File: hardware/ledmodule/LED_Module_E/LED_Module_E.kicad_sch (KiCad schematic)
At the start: 86 parts, among them J1 USB4125-GF-A, J2 Conn_02x11_Odd_Even, Q1 Si3456DDV, Q11 Si3456DDV, Q12 Si3456DDV, Q2 Si3456DDV, Q3 Si3456DDV, Q4 Si3456DDV, Q5 Si3456DDV, Q6 Si3456DDV, Q7 Si3456DDV, Q8 Si3456DDV, U1 TMP1075DGK, U2 74HCT244, U3 24AA02UIDT-I/OT

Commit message: Fix / add meta data in title_block for all LED modules.
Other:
- title: (none) -> besteLampe! LED Module E
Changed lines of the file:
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@@
 	(generator_version "8.0")
 	(paper "A4")
+	(title_block
+		(title "besteLampe! LED Module E")
+		(date "2024-07-01")
+		(rev "1.0")
+		(comment 1 "See  https://lenaschimmel.de/besteLampe! for the source and more information")
+		(comment 2 "This source describes Open Hardware and is licensed under the CERN-OHL-S v2.")
+		(comment 3 "Copyright 2024 Lena Schimmel <mail@lenaschimmel.de>")
+	)
 	(junction
 		(at 160.655 138.43)

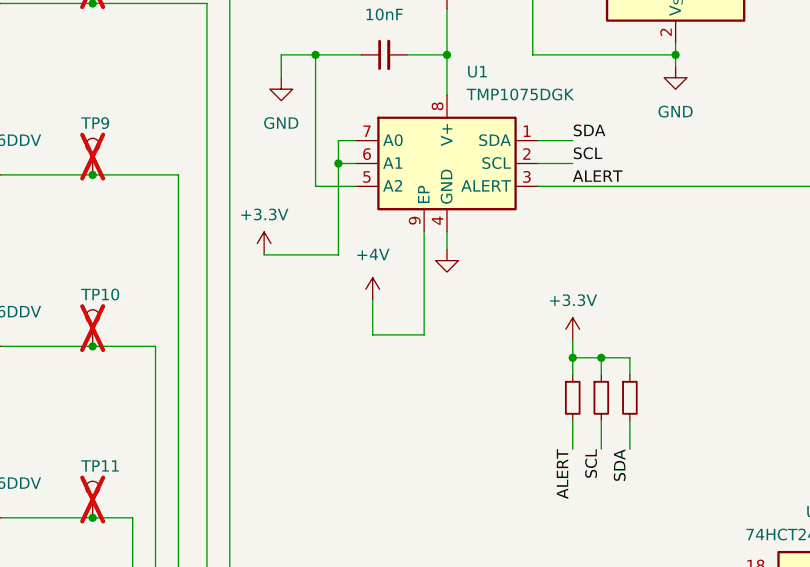
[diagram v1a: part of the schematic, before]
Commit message: Probably minor changes (specific R values, etc.)
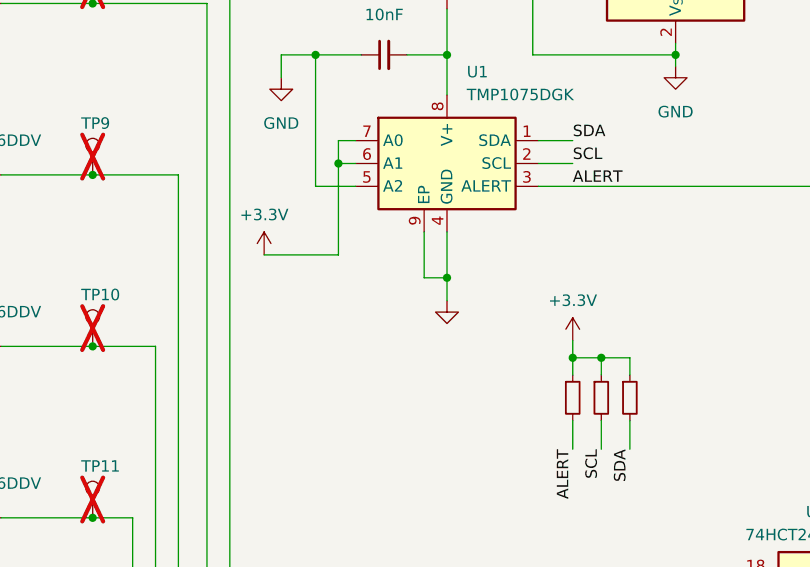
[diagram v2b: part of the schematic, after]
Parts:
- R10, R13, R14, R15, R16, R17, R18, R19, R20, R21, R22, R23, R24, R25, R26, R27, R28, R29, R30, R9: value R_Small -> 2740R
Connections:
- net +4V: no longer U1.9 (EP)
- net GND: now also U1.9 (EP)
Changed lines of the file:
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@@
 	)
 	(junction
+		(at 146.05 76.2)
+		(diameter 0)
+		(color 0 0 0 0)
+	)
+	(junction
 		(at 226.06 116.84)
 		(diameter 0)
@@
 	(wire
 		(pts
+			(xy 143.51 76.2) (xy 146.05 76.2)
+		)
+		(stroke
+			(width 0)
+			(type default)
+		)
+	)
+	(wire
+		(pts
 			(xy 171.45 50.165) (xy 171.45 51.435)
 		)
@@
 	(wire
 		(pts
+			(xy 146.05 76.2) (xy 146.05 78.74)
+		)
+		(stroke
+			(width 0)
+			(type default)
+		)
+	)
+	(wire
+		(pts
 			(xy 147.955 114.3) (xy 116.205 114.3)
 		)
@@
 	(wire
 		(pts
-			(xy 137.795 82.55) (xy 137.795 78.74)
-		)
-		(stroke
-			(width 0)
-			(type default)
-		)
-	)
-	(wire
-		(pts
 			(xy 67.31 76.2) (xy 81.915 76.2)
 		)
@@
 	(wire
 		(pts
-			(xy 143.51 82.55) (xy 137.795 82.55)
-		)
-		(stroke
-			(width 0)
-			(type default)
-		)
-	)
-	(wire
-		(pts
 			(xy 203.2 111.76) (xy 219.71 111.76)
 		)
@@
 	(wire
 		(pts
-			(xy 143.51 71.12) (xy 143.51 82.55)
-		)
-		(stroke
-			(width 0)
-			(type default)
-		)
-	)
-	(wire
-		(pts
 			(xy 144.78 135.89) (xy 144.78 138.43)
 		)
@@
 	(wire
 		(pts
+			(xy 143.51 71.12) (xy 143.51 76.2)
+		)
+		(stroke
+			(width 0)
+			(type default)
+		)
+	)
+	(wire
+		(pts
 			(xy 222.885 114.3) (xy 222.885 130.81)
 		)
@@
 	(wire
 		(pts
-			(xy 146.05 71.12) (xy 146.05 73.025)
+			(xy 146.05 71.12) (xy 146.05 76.2)
 		)
 		(stroke
@@
 			)
 		)
-		(property "Value" "R_Small"
+		(property "Value" "2740R"
 			(at 209.5499 136.525 0)
 			(effects
@@
 			)
 		)
-		(property "Value" "R_Small"
+		(property "Value" "2740R"
 			(at 150.495 134.6199 0)
 			(effects
@@
 			)
 		)
-		(property "Value" "R_Small"
+		(property "Value" "2740R"
 			(at 153.67 134.6199 0)
 			(effects
@@
 	)
 	(symbol
-		(lib_id "power:+4V")
-		(at 137.795 78.74 0)
-		(unit 1)
-		(exclude_from_sim no)
-		(in_bom yes)
-		(on_board yes)
-		(dnp no)
-		(fields_autoplaced yes)
-		(property "Reference" "#PWR017"
-			(at 137.795 82.55 0)
-			(effects
-				(font
-					(size 1.27 1.27)
-				)
-				(hide yes)
-			)
-		)
-		(property "Value" "+4V"
-			(at 137.795 73.66 0)
-			(effects
-				(font
-					(size 1.27 1.27)
-				)
-			)
-		)
-		(property "Footprint" ""
-			(at 137.795 78.74 0)
-			(effects
-				(font
-					(size 1.27 1.27)
-				)
-				(hide yes)
-			)
-		)
-		(property "Datasheet" ""
-			(at 137.795 78.74 0)
-			(effects
-				(font
-					(size 1.27 1.27)
-				)
-				(hide yes)
-			)
-		)
-		(property "Description" "Power symbol creates a global label with name \"+4V\""
-			(at 137.795 78.74 0)
-			(effects
-				(font
-					(size 1.27 1.27)
-				)
-				(hide yes)
-			)
-		)
-		(pin "1"
-		)
-		(instances
-			(project "LED_Module_E"
-				(path "/271a71a9-d0cc-4466-ad75-113fb931f3c8"
-					(reference "#PWR017")
-					(unit 1)
-				)
-			)
-		)
-	)
-	(symbol
 		(lib_id "Device:R")
 		(at 76.2 116.84 90)
@@
 			)
 		)
-		(property "Value" "R_Small"
+		(property "Value" "2740R"
 			(at 168.91 90.8049 0)
 			(effects
@@
 			)
 		)
-		(property "Value" "R_Small"
+		(property "Value" "2740R"
 			(at 234.95 134.6199 0)
 			(effects
@@
 			)
 		)
-		(property "Value" "R_Small"
+		(property "Value" "2740R"
 			(at 166.37 134.6199 0)
 			(effects
@@
 			)
 		)
-		(property "Value" "R_Small"
+		(property "Value" "2740R"
 			(at 228.6 134.6199 0)
 			(effects
@@
 			)
 		)
-		(property "Value" "R_Small"
+		(property "Value" "2740R"
 			(at 165.735 90.8049 0)
 			(effects
@@
 			)
 		)
-		(property "Value" "R_Small"
+		(property "Value" "2740R"
 			(at 162.56 90.8049 0)
 			(effects
@@
 			)
 		)
-		(property "Value" "R_Small"
+		(property "Value" "2740R"
 			(at 238.125 134.6199 0)
 			(effects
@@
 	(symbol
 		(lib_id "power:GND")
-		(at 146.05 73.025 0)
+		(at 146.05 78.74 0)
 		(unit 1)
 		(exclude_from_sim no)
@@
 		(fields_autoplaced yes)
 		(property "Reference" "#PWR01"
-			(at 146.05 79.375 0)
+			(at 146.05 85.09 0)
 			(effects
 				(font
@@
 		)
 		(property "Value" "GND"
-			(at 146.05 78.105 0)
+			(at 146.05 83.82 0)
 			(effects
 				(font
@@
 		)
 		(property "Footprint" ""
-			(at 146.05 73.025 0)
+			(at 146.05 78.74 0)
 			(effects
 				(font
@@
 		)
 		(property "Datasheet" ""
-			(at 146.05 73.025 0)
+			(at 146.05 78.74 0)
 			(effects
 				(font
@@
 		)
 		(property "Description" "Power symbol creates a global label with name \"GND\" , ground"
-			(at 146.05 73.025 0)
+			(at 146.05 78.74 0)
 			(effects
 				(font
@@
 			)
 		)
-		(property "Value" "R_Small"
+		(property "Value" "2740R"
 			(at 225.425 134.6199 0)
 			(effects
@@
 			)
 		)
-		(property "Value" "R_Small"
+		(property "Value" "2740R"
 			(at 144.145 134.6199 0)
 			(effects
@@
 			)
 		)
-		(property "Value" "R_Small"
+		(property "Value" "2740R"
 			(at 160.02 134.6199 0)
 			(effects
@@
 			)
 		)
-		(property "Value" "R_Small"
+		(property "Value" "2740R"
 			(at 222.25 134.6199 0)
 			(effects
@@
 			)
 		)
-		(property "Value" "R_Small"
+		(property "Value" "2740R"
 			(at 147.32 134.6199 0)
 			(effects
@@
 			)
 		)
-		(property "Value" "R_Small"
+		(property "Value" "2740R"
 			(at 156.845 134.6199 0)
 			(effects
@@
 			)
 		)
-		(property "Value" "R_Small"
+		(property "Value" "2740R"
 			(at 219.075 134.6199 0)
 			(effects
@@
 			)
 		)
-		(property "Value" "R_Small"
+		(property "Value" "2740R"
 			(at 163.195 134.6199 0)
 			(effects
@@
 			)
 		)
-		(property "Value" "R_Small"
+		(property "Value" "2740R"
 			(at 231.775 134.6199 0)
 			(effects
@@
 			)
 		)
-		(property "Value" "R_Small"
+		(property "Value" "2740R"
 			(at 241.3 134.6199 0)
 			(effects

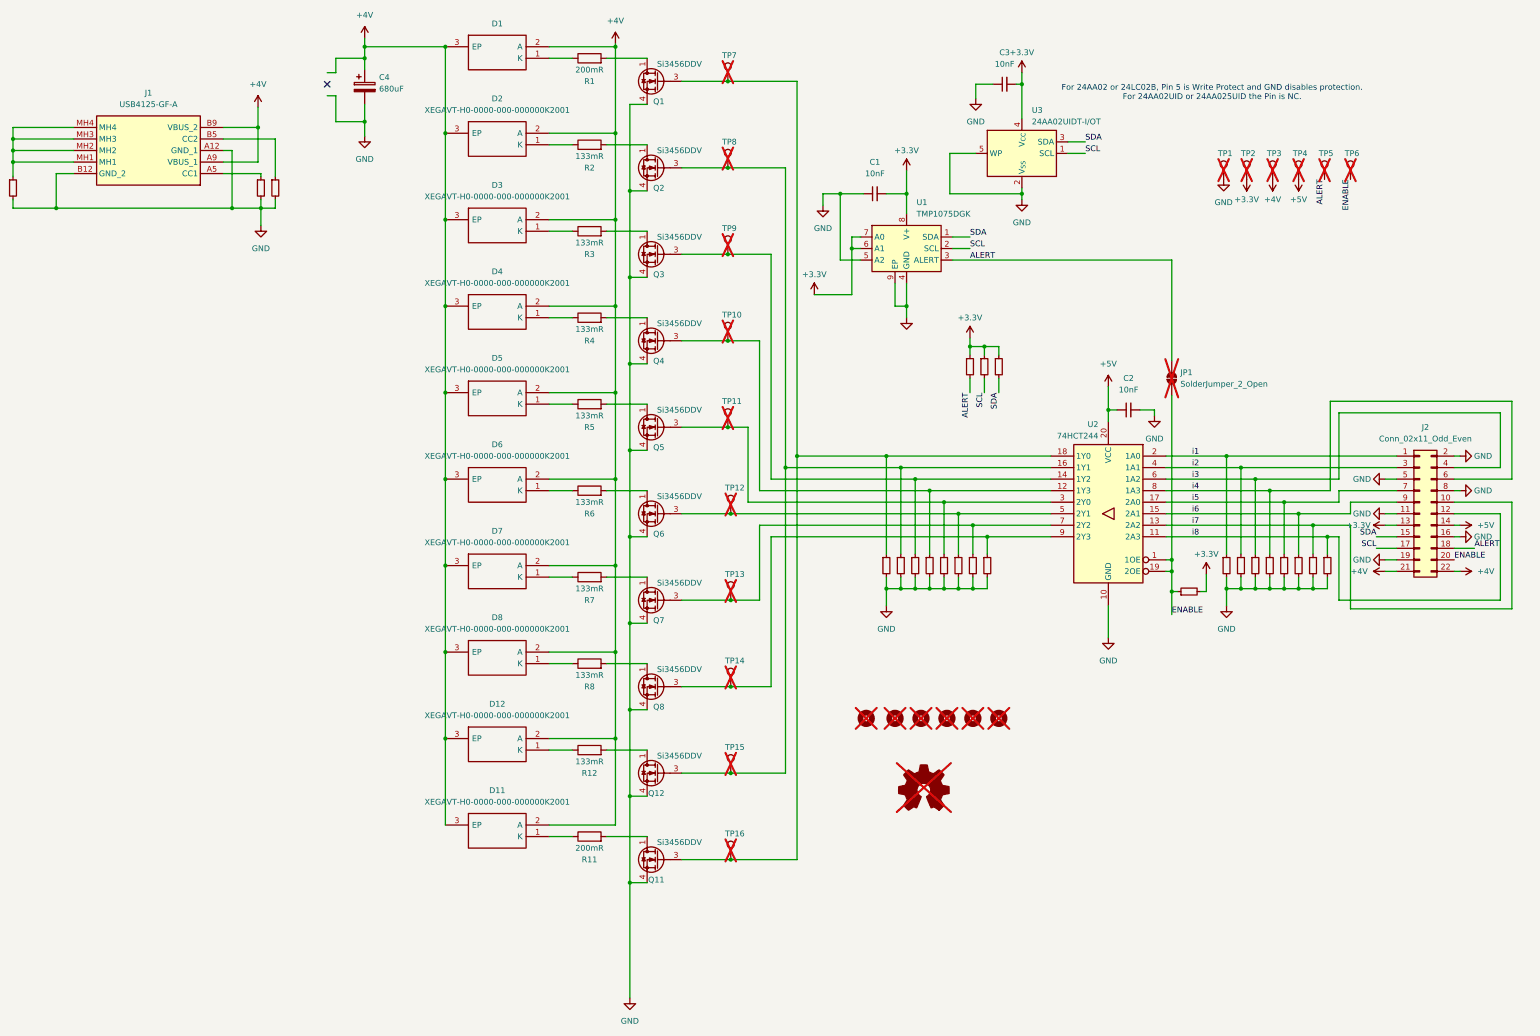
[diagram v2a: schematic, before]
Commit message: Complete redesign of LED Module E for the ABL.
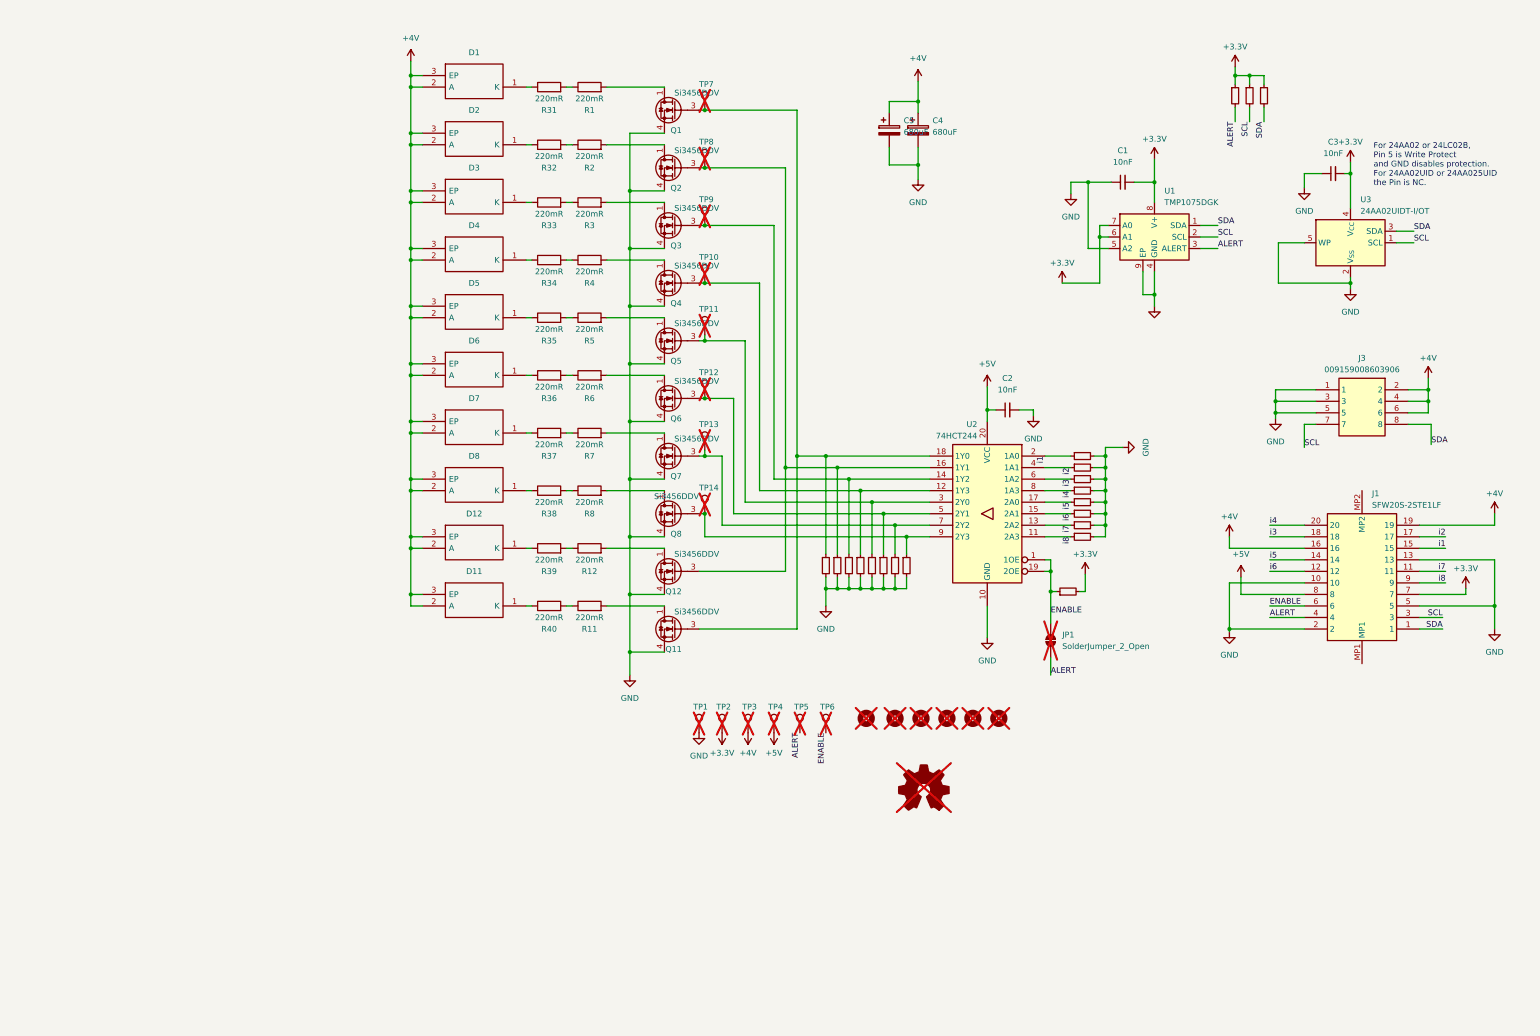
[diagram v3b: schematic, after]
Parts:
- removed J1: USB4125-GF-A, USB4125-GF-A:USB4125GFA, symbol USB4125-GF-A:USB4125-GF-A
- removed J2: Conn_02x11_Odd_Even, TSM-111-01-T-DV:TSM-111-YY-ZZZ-DV, symbol Connector_Generic:Conn_02x11_Odd_Even
- removed R31, R32, R33: 5100R, Resistor_SMD:R_0603_1608Metric, symbol Device:R_Small
- removed TP15, TP16: TestPoint, TestPoint:TestPoint_Pad_D1.0mm, symbol Connector:TestPoint
- added C5: 680uF, Capacitor_SMD:CP_Elec_10x7.9, symbol Device:C_Polarized
- added J1: SFW20S-2STE1LF, SFW20S2STE1LF, symbol SFW20S-2STE1LF:SFW20S-2STE1LF
- added J3: 009159008603906, 009159008603906, symbol 009159008603906:009159008603906
- added R31, R32, R33, R34, R35, R36, R37, R38, R39, R40: 220mR, Resistor_SMD:R_1020_2550Metric, symbol Device:R
- LOGO1: footprint Symbol:OSHW-Logo_7.5x8mm_Copper -> Symbol:OSHW-Logo_5.7x6mm_SilkScreen
- R1, R11: value 200mR -> 220mR
- R10, R13, R14, R15, R16, R17, R18, R19, R20, R21, R22, R23, R24, R25, R26, R27, R28, R29, R30, R9: footprint Resistor_SMD:R_0805_2012Metric_Pad1.20x1.40mm_HandSolder -> Resistor_SMD:R_0603_1608Metric
- R12, R2, R3, R4, R5, R6, R7, R8: value 133mR -> 220mR
- TP1, TP2, TP3, TP4, TP5, TP6: footprint TestPoint:TestPoint_THTPad_D1.0mm_Drill0.5mm -> TestPoint:TestPoint_Pad_D1.0mm
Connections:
- net +3.3V: now also J1.7
- net +4V: now also C5.1, J1.16, J1.19, J3.2, J3.4, J3.6
- net +5V: now also J1.8
- net ALERT: now also J1.4
- net ENABLE: now also J1.6
- net GND: now also C5.2, J1.10, J1.13, J1.2, J1.5, J3.1, J3.3, J3.5
- net SCL: now also J1.3, J3.7
- net SDA: now also J1.1, J3.8
- net i1: now also J1.15
- net i2: now also J1.17
- net i3: now also J1.18
- net i4: now also J1.20
- net i5: now also J1.14
- net i6: now also J1.12
- net i7: now also J1.11
- net i8: now also J1.9
- net at D7.1 (K): now also R37.1; no longer R7.1
- net at D8.1 (K): now also R38.1; no longer R8.1
- net at R11.1: now also R40.2; no longer D11.1 (K)
- net at D6.1 (K): now also R36.1; no longer R6.1
- net at D12.1 (K): now also R39.1; no longer R12.1
- net at D1.1 (K): now also R31.1; no longer R1.1
- net at R5.1: now also R35.2; no longer D5.1 (K)
- net at D2.1 (K): now also R32.1; no longer R2.1
- net at D4.1 (K): now also R34.1; no longer R4.1
- net at D3.1 (K): now also R33.1; no longer R3.1
- new net: R38.2, R8.1
- new net: R36.2, R6.1
- new net: R34.2, R4.1
- new net: R12.1, R39.2
- new net: R37.2, R7.1
- new net: D5.1 (K), R35.1
- new net: D11.1 (K), R40.1
- new net: R1.1, R31.2
- new net: R2.1, R32.2
- new net: R3.1, R33.2
- no-connect marks 1 -> 0
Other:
- moved on the sheet: C1, C2, C3, C4, D1, JP1, Q1, Q11, Q12, Q2, Q3, Q4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

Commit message: Mirror the connector, optimize VLED between connector and LEDs.
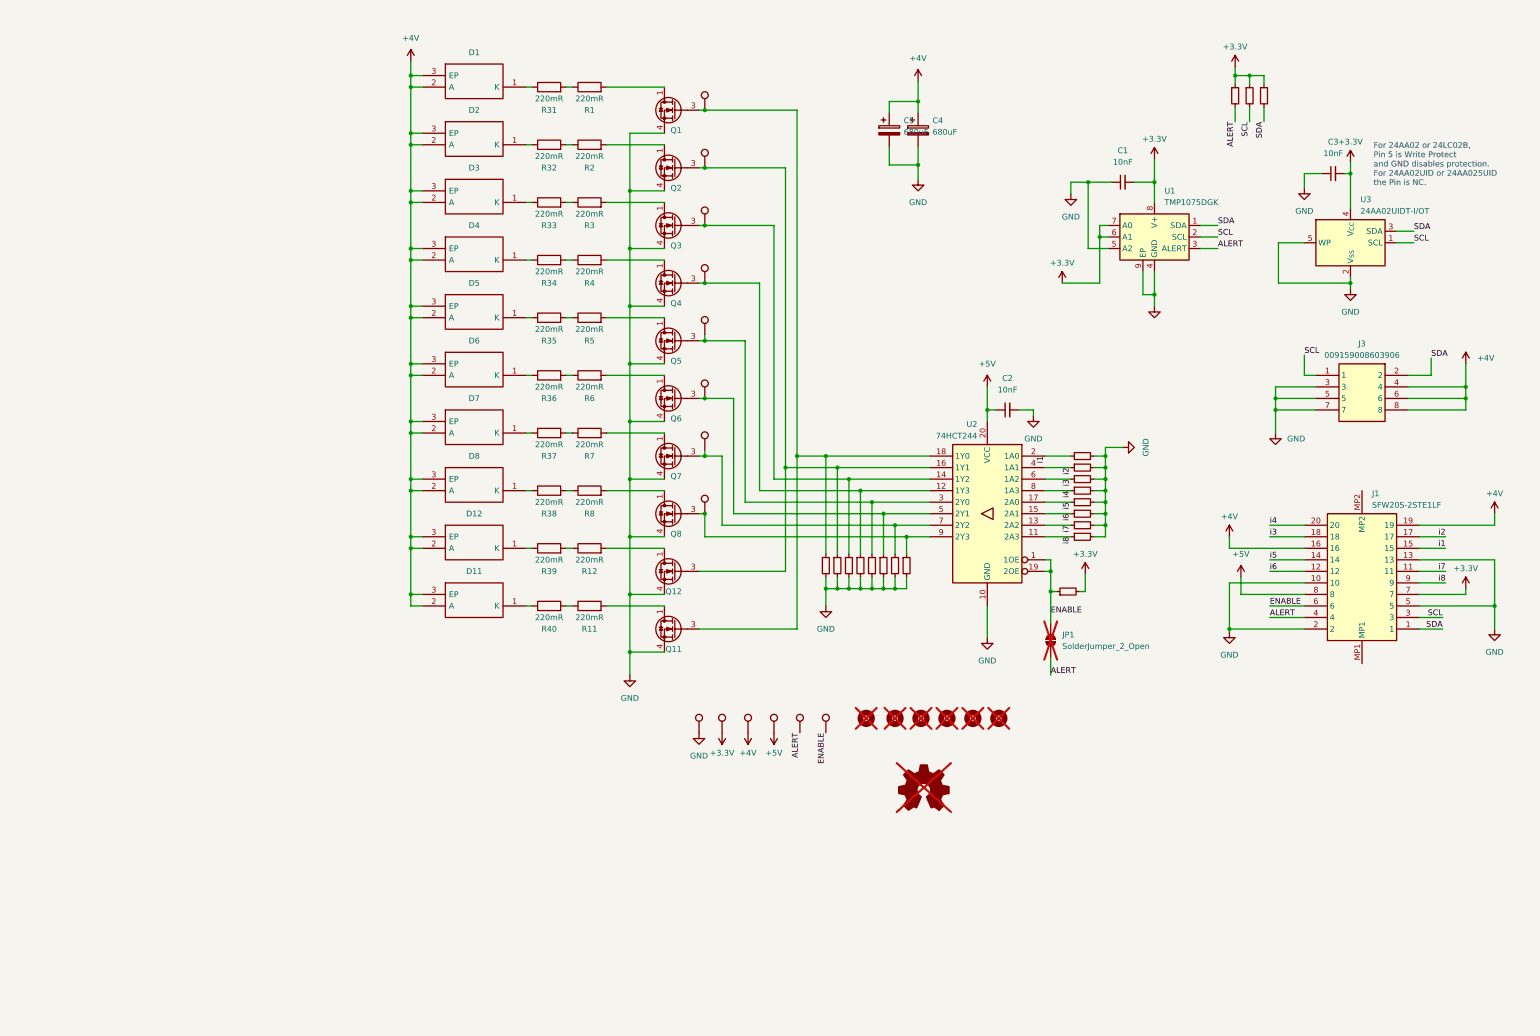
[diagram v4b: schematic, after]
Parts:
- TP1, TP10, TP11, TP12, TP13, TP14, TP2, TP3, TP4, TP5, TP6, TP7, TP8, TP9: now fitted
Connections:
- net +4V: now also J3.8; no longer J3.2
- net GND: now also J3.7; no longer J3.1
- net SCL: now also J3.1; no longer J3.7
- net SDA: now also J3.2; no longer J3.8
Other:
- moved on the sheet: J3
